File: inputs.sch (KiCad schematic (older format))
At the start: 36 parts

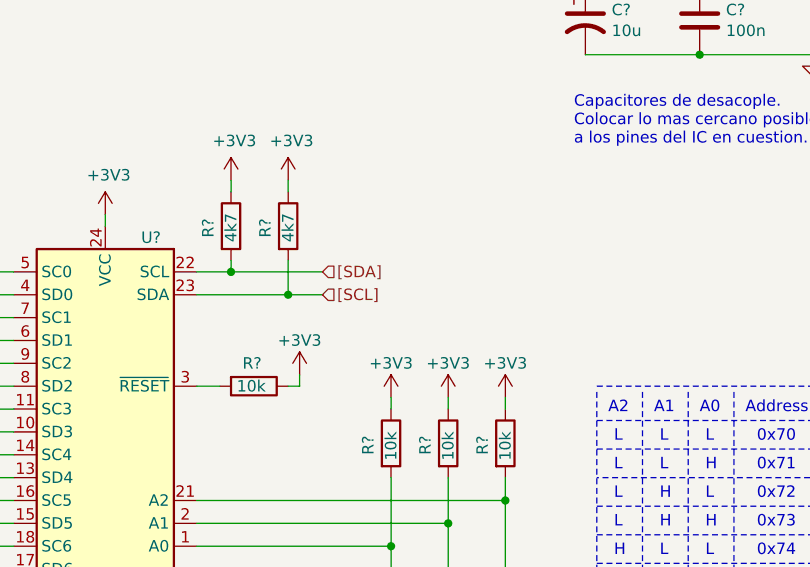
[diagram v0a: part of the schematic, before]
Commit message: Arreglos.
    * Arreglo referencias de address de salida(PCF8574)
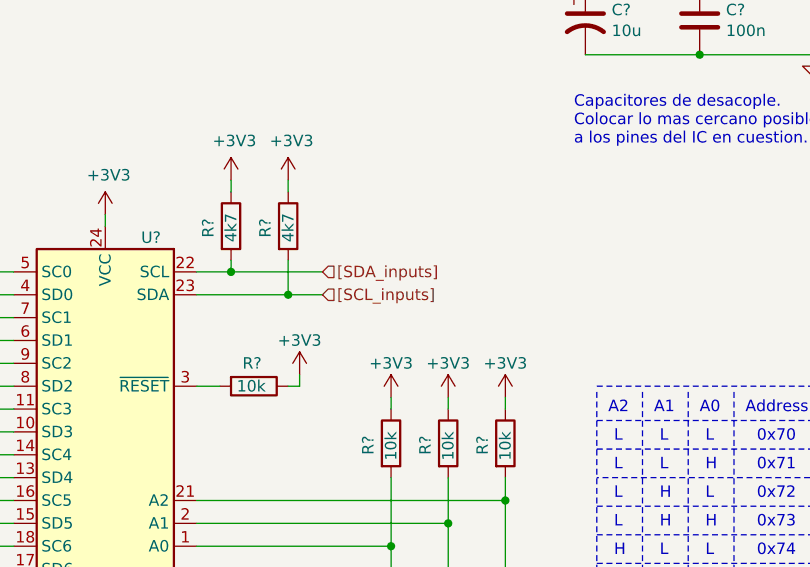
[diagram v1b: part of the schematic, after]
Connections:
- net [SCL] renamed [SCL_inputs]
- net [SDA] renamed [SDA_inputs]
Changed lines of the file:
@@
 $Descr A4 11693 8268
 encoding utf-8
-Sheet 4 5
+Sheet 3 5
 Title ""
 Date ""
@@
 	1    0    0    1
 $EndComp
-Text HLabel 7400 3300 2    50   Input ~ 0
-[SDA]
 Text HLabel 7400 3400 2    50   Input ~ 0
-[SCL]
+[SCL_inputs]
 $Comp
 L 00_lib_sch:Interface_Expansion_TCA9548APWR U?
@@
 	1    0    0    -1
 $EndComp
+Text HLabel 7400 3300 2    50   Input ~ 0
+[SDA_inputs]
 $EndSCHEMATC
